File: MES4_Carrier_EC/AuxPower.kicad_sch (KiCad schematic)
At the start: 42 parts, among them J14 IMU 9V, J15 SERVO 24V, J16 SCREEN 5V, J17 SERVO UART, SW2 SS12D10G5, U10 URB2405YMD-20WR3, U9 URB2409S-10WR3

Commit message: One ground and a 4-layer board
- GND_24V merged into GND (ONE_GND in gen.py): every GND_24V power symbol
  becomes GND, net tie NT1 left out, notes reworded. Symbol UUIDs unchanged,
  so every footprint keeps its link.
- 4 layers, JLC04161H-7628 stackup (1.6 mm, ENIG): Top Signal / GND plane
  (In1) / +24V plane (In2) / Bottom Signal.
- Net classes: Out_3A (1.5 mm) for +24V_SRV, +5V_SCR, VBUS_SCR; +24V_AUX to
  24V_Power; +5V_SRV, +9V_IMU, IMU_9V to Power; INA236 shunt pattern fixed
  (Net-(U*-IN-)).
- J1's NPTH holes back to F&B.Cu as in its library footprint.

ERC 0, checks passed, DRC 11 silkscreen warnings, schematic parity clean.

Co-Authored-By: Claude Opus 5.5 <noreply@anthropic.com>
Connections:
- net GND_24V is gone; now on net GND: C26.2, C27.2, C28.2, C30.2, C31.2, C32.2, J15.2 (Pin_2), U10.2 (-Vin), U9.1 (GND)
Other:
- note added: "L2 10 µH (same part as L1) + C26 / C27: a pi filter of its own for the IMU and screen converters, so the screen's 20 W converter neither loads nor disturbs the logic supply (L1, Power sheet). Load at 24 V: IMU ≤ 0.5 A + screen ≤ 0.95 A ≈ 1.45 A; L2 is rated 2.1 A (2.9 A saturation). Both converters are isolated modules; on this board their input and output sides share the one GND (as the logic DC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"
- note removed: "L2 10 µH (same part as L1) + C26 / C27: a pi filter of its own for the IMU and screen converters, so the screen's 20 W converter neither loads nor disturbs the logic supply (L1, Power sheet). Load at 24 V: IMU ≤ 0.5 A + screen ≤ 0.95 A ≈ 1.45 A; L2 is rated 2.1 A (2.9 A saturation). Both converters are isolated: input side on GND_24V, output side on GND (same scheme as the logic DC/DC)."

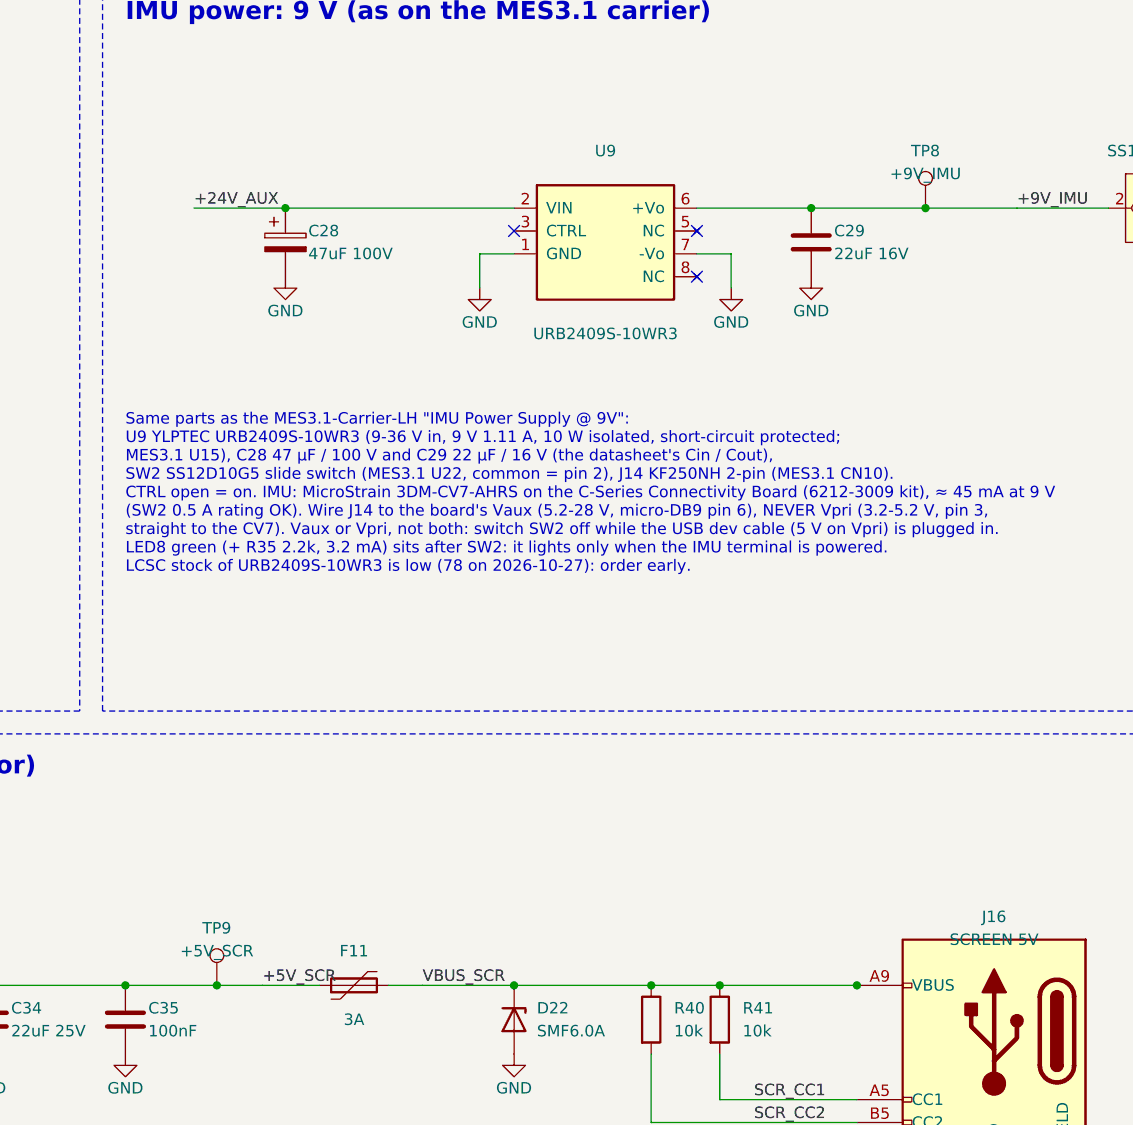
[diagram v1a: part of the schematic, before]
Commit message: Placement and silkscreen pass: ADS by the load-cell inputs, test points, logo
- Left column top to bottom: ADS1232 under J12/J13 (input filter toward the
  connectors), STDC14 + ESD grid, then the MES4-MCU slot moved down 22.3 mm;
  RESET (SW1) beside J1 with the 5 V socket caps C8/C9.
- Test points named by what they feed (TP_NAME in gen.py: 24V, 24V FILT,
  5V MAIN, 5V MCU, 3V3, 9V IMU, 5V SCREEN); bottom row in a Flasher-style
  rounded box, 24V/GND under the XT30, 5V SCREEN/GND by the screen USB-C.
- Supply LEDs centred between SW2 and the winch block; short knockout labels
  all one box size (drawn as cut-out silk shapes).
- + at the anode of every two-pin diode and LED; SW2 marked IMU PWR with
  OFF/ON (slider toward pin 1 = on); mounting-hole refs off the silkscreen.
- Sensor inputs in the column under L1/L2, U10 output caps against U10,
  servo support parts in the square by J17, FE-URT-2 J17/J15 label boxes,
  Monkey Robotics logo (43 x 9.3 mm) in the freed space.

ERC 0, DRC 14 silkscreen warnings (13 edge, J1 circle), schematic parity clean.

Co-Authored-By: Claude Opus 5.5 <noreply@anthropic.com>
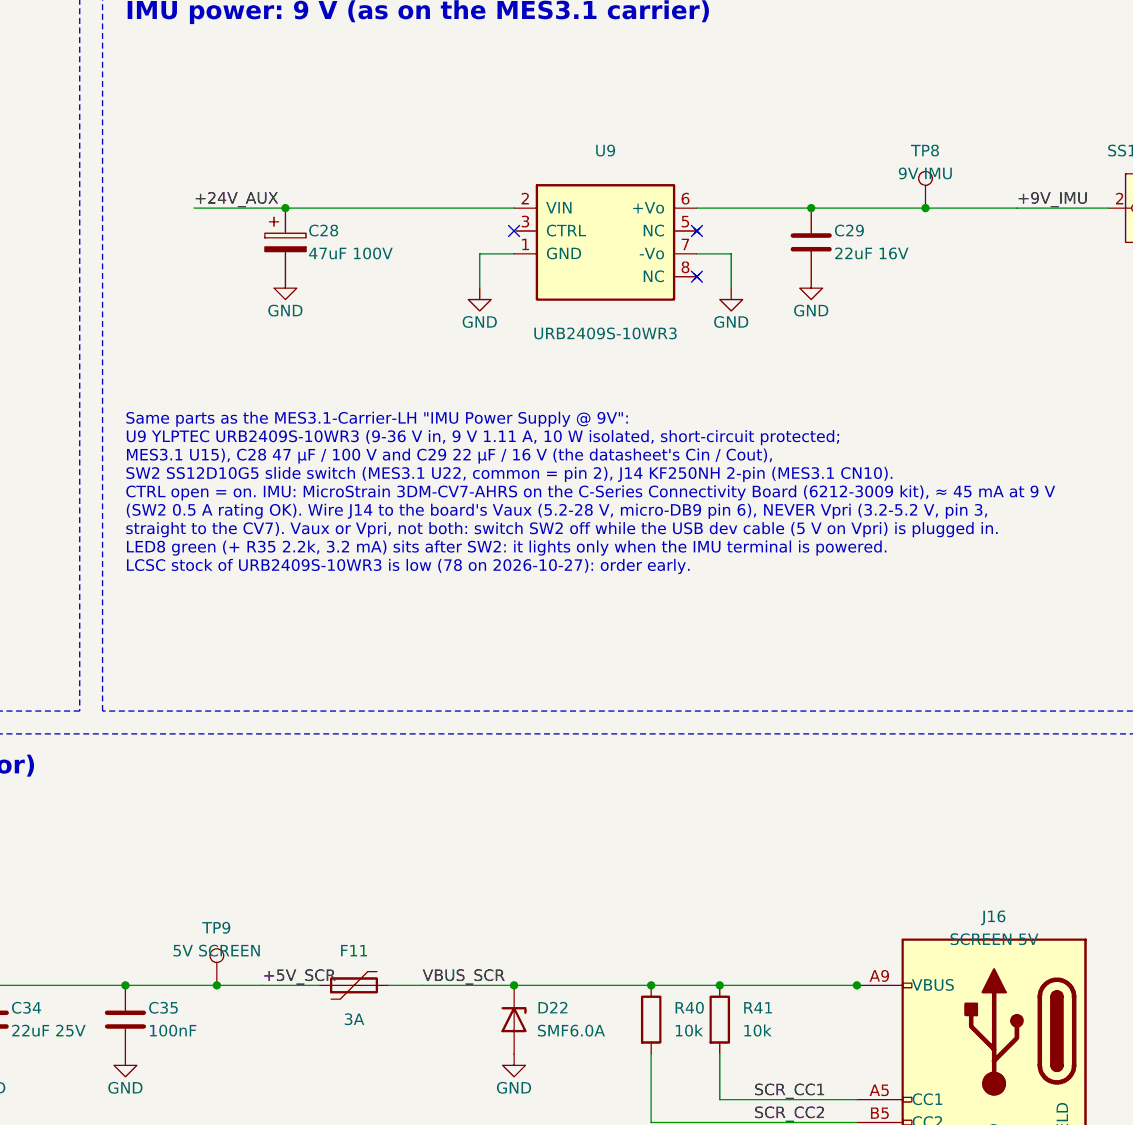
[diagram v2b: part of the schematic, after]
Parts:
- TP8: value +9V_IMU -> 9V IMU
- TP9: value +5V_SCR -> 5V SCREEN
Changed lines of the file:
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@@
 			(effects (font (size 1.27 1.27)))
 		)
-		(property "Value" "+9V_IMU"
+		(property "Value" "9V IMU"
 			(at 213.36 41.91 0)
 			(effects (font (size 1.27 1.27)))
@@
 			(effects (font (size 1.27 1.27)))
 		)
-		(property "Value" "+5V_SCR"
+		(property "Value" "5V SCREEN"
 			(at 134.62 128.27 0)
 			(effects (font (size 1.27 1.27)))

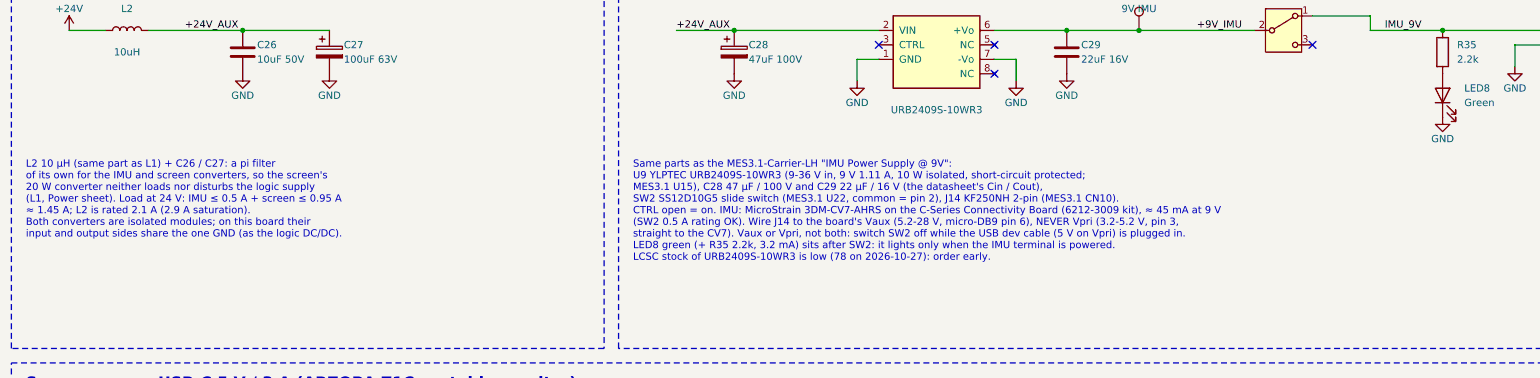
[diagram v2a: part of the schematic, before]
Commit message: Fix design review R3 findings: U9 part, stale LCSC fields, labels, J16
- B1: U9 is now YLPTEC URB2409S-6WR3 (C7468814, 9 V 6 W) on U1's
  footprint; the 10 W URB2409S-10WR3 isn't in JLC's assembly library.
  The production BOM had a 5 V module at U9 and the wrong SW2 because
  EasyEDA footprints carry an "LCSC Part" field the Fabrication Toolkit
  reads first: libs.py strips it (and the unprintable pin-1 dots it was
  copying back), and the new parts_sync.py syncs board footprints,
  values, fields and BOM flags from the schematic. TP1-TP9 and H2-H5
  are out of the BOM and CPL.
- M2 / L5: "5V LOAD CELL" across J12 / J13; "CANBUS" knockout by J4.
- B2: J16 moves 1.25 mm west so its mouth reaches the board edge.
- B8 / N6: README (one ground, U9, J16, labels, TPs), schematic notes
  and HANDOFF updated; 1:1 A4 print refreshed.
- DRC with parity at the 3 accepted J4 notes; nets, audit, DFM clean.
  production/ is stale until the Fabrication Toolkit is re-run.

Co-Authored-By: Claude Opus 5.5 <noreply@anthropic.com>
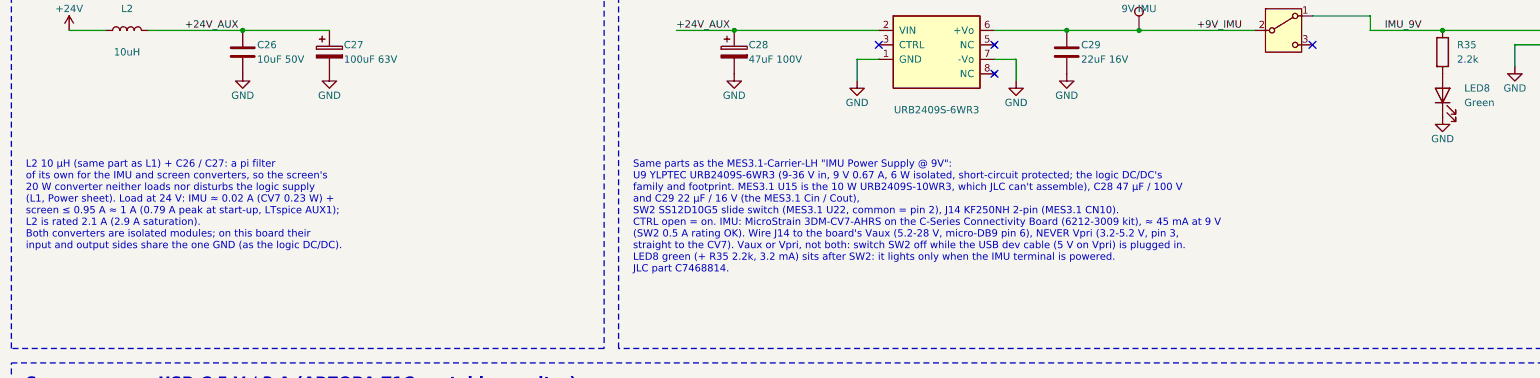
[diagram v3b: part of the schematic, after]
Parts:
- TP8, TP9: now left out of the parts list
- U9: value URB2409S-10WR3 -> URB2409S-6WR3; footprint MES4-Carrier-EC:PWRM-TH_YLPTEC_URBXXXXS-10WR3 -> MES4-Carrier-EC:PWRM-TH_YLPTEC_URXXXXXS-6WR3; symbol MES4-Carrier-EC:URB2409S-10WR3 -> MES4-Carrier-EC:URB2409S-6WR3; LCSC C7424703 -> C7468814
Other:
- note added: "L2 10 µH (same part as L1) + C26 / C27: a pi filter of its own for the IMU and screen converters, so the screen's 20 W converter neither loads nor disturbs the logic supply (L1, Power sheet). Load at 24 V: IMU ≈ 0.02 A (CV7 0.23 W) + screen ≤ 0.95 A ≈ 1 A (0.79 A peak at start-up, LTspice AUX1); L2 is rated 2.1 A (2.9 A saturation). Both converters are isolated modules; on this board their input 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"
- note added: "Same parts as the MES3.1-Carrier-LH "IMU Power Supply @ 9V": U9 YLPTEC URB2409S-6WR3 (9-36 V in, 9 V 0.67 A, 6 W isolated, short-circuit protected; the logic DC/DC's family and footprint. MES3.1 U15 is the 10 W URB2409S-10WR3, which JLC can't assemble), C28 47 µF / 100 V and C29 22 µF / 16 V (the MES3.1 Cin / Cout), SW2 SS12D10G5 slide switch (MES3.1 U22, common = pin 2), J14 KF250NH 2-pin (MES3.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"
- note removed: "L2 10 µH (same part as L1) + C26 / C27: a pi filter of its own for the IMU and screen converters, so the screen's 20 W converter neither loads nor disturbs the logic supply (L1, Power sheet). Load at 24 V: IMU ≤ 0.5 A + screen ≤ 0.95 A ≈ 1.45 A; L2 is rated 2.1 A (2.9 A saturation). Both converters are isolated modules; on this board their input and output sides share the one GND (as the logic DC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"
- note removed: "Same parts as the MES3.1-Carrier-LH "IMU Power Supply @ 9V": U9 YLPTEC URB2409S-10WR3 (9-36 V in, 9 V 1.11 A, 10 W isolated, short-circuit protected; MES3.1 U15), C28 47 µF / 100 V and C29 22 µF / 16 V (the datasheet's Cin / Cout), SW2 SS12D10G5 slide switch (MES3.1 U22, common = pin 2), J14 KF250NH 2-pin (MES3.1 CN10). CTRL open = on. IMU: MicroStrain 3DM-CV7-AHRS on the C-Series Connectivity Bo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"
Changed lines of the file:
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@@
 		(effects (font (size 1.27 1.27)) (justify left bottom))
 	)
-	(text "L2 10 µH (same part as L1) + C26 / C27: a pi filter\nof its own for the IMU and screen converters, so the screen's\n20 W converter neither loads nor disturbs the logic supply\n(L1, Power sheet). Load at 24 V: IMU ≤ 0.5 A + screen ≤ 0.95 A\n≈ 1.45 A; L2 is rated 2.1 A (2.9 A saturation).\nBoth converters are isolated modules; on this board their\ninput and output sides share the one GND (as the logic DC/DC)."
+	(text "L2 10 µH (same part as L1) + C26 / C27: a pi filter\nof its own for the IMU and screen converters, so the screen's\n20 W converter neither loads nor disturbs the logic supply\n(L1, Power sheet). Load at 24 V: IMU ≈ 0.02 A (CV7 0.23 W) +\nscreen ≤ 0.95 A ≈ 1 A (0.79 A peak at start-up, LTspice AUX1);\nL2 is rated 2.1 A (2.9 A saturation).\nBoth converters are isolated modules; on this board their\ninput and output sides share the one GND (as the logic DC/DC)."
 		(exclude_from_sim no)
 		(at 17.78 68.58 0)
@@
 		(stroke (width 0) (type default))
 	)
-	(text "Same parts as the MES3.1-Carrier-LH \"IMU Power Supply @ 9V\":\nU9 YLPTEC URB2409S-10WR3 (9-36 V in, 9 V 1.11 A, 10 W isolated, short-circuit protected;\nMES3.1 U15), C28 47 µF / 100 V and C29 22 µF / 16 V (the datasheet's Cin / Cout),\nSW2 SS12D10G5 slide switch (MES3.1 U22, common = pin 2), J14 KF250NH 2-pin (MES3.1 CN10).\nCTRL open = on. IMU: MicroStrain 3DM-CV7-AHRS on the C-Series Connectivity Board (6212-3009 kit), ≈ 45 mA at 9 V\n(SW2 0.5 A rating OK). Wire J14 to the board's Vaux (5.2-28 V, micro-DB9 pin 6), NEVER Vpri (3.2-5.2 V, pin 3,\nstraight to the CV7). Vaux or Vpri, not both: switch SW2 off while the USB dev cable (5 V on Vpri) is plugged in.\nLED8 green (+ R35 2.2k, 3.2 mA) sits after SW2: it lights only when the IMU terminal is powered.\nLCSC stock of URB2409S-10WR3 is low (78 on 2026-10-27): order early."
+	(text "Same parts as the MES3.1-Carrier-LH \"IMU Power Supply @ 9V\":\nU9 YLPTEC URB2409S-6WR3 (9-36 V in, 9 V 0.67 A, 6 W isolated, short-circuit protected; the logic DC/DC's\nfamily and footprint. MES3.1 U15 is the 10 W URB2409S-10WR3, which JLC can't assemble), C28 47 µF / 100 V\nand C29 22 µF / 16 V (the MES3.1 Cin / Cout),\nSW2 SS12D10G5 slide switch (MES3.1 U22, common = pin 2), J14 KF250NH 2-pin (MES3.1 CN10).\nCTRL open = on. IMU: MicroStrain 3DM-CV7-AHRS on the C-Series Connectivity Board (6212-3009 kit), ≈ 45 mA at 9 V\n(SW2 0.5 A rating OK). Wire J14 to the board's Vaux (5.2-28 V, micro-DB9 pin 6), NEVER Vpri (3.2-5.2 V, pin 3,\nstraight to the CV7). Vaux or Vpri, not both: switch SW2 off while the USB dev cable (5 V on Vpri) is plugged in.\nLED8 green (+ R35 2.2k, 3.2 mA) sits after SW2: it lights only when the IMU terminal is powered.\nJLC part C7468814."
 		(exclude_from_sim no)
 		(at 124.46 68.58 0)
@@
 	)
 	(symbol
-		(lib_id "MES4-Carrier-EC:URB2409S-10WR3")
+		(lib_id "MES4-Carrier-EC:URB2409S-6WR3")
 		(at 177.8 48.26 0)
 		(unit 1)
@@
 			(effects (font (size 1.27 1.27)))
 		)
-		(property "Value" "URB2409S-10WR3"
+		(property "Value" "URB2409S-6WR3"
 			(at 177.8 59.69 0)
 			(effects (font (size 1.27 1.27)))
 		)
-		(property "Footprint" "MES4-Carrier-EC:PWRM-TH_YLPTEC_URBXXXXS-10WR3"
+		(property "Footprint" "MES4-Carrier-EC:PWRM-TH_YLPTEC_URXXXXXS-6WR3"
 			(at 177.8 48.26 0)
 			(effects (font (size 1.27 1.27)) (hide yes))
 		)
-		(property "Datasheet" "https://www.lcsc.com/product-detail/C7424703.html"
+		(property "Datasheet" "https://www.lcsc.com/product-detail/C7468814.html"
 			(at 177.8 48.26 0)
 			(effects (font (size 1.27 1.27)) (hide yes))
 		)
-		(property "Description" "IMU supply, YLPTEC URB2409S-10WR3: 24 V to 9 V 1.11 A, 10 W isolated (as U15 on the MES3.1 carrier)"
+		(property "Description" "IMU supply, YLPTEC URB2409S-6WR3: 24 V to 9 V 0.67 A, 6 W isolated, SIP-8 (the logic DC/DC's family and footprint; the MES3.1 carrier's 10 W URB2409S-10WR3, C7424703, is not in JLC's assembly library)"
 			(at 177.8 48.26 0)
 			(effects (font (size 1.27 1.27)) (hide yes))
 		)
-		(property "LCSC" "C7424703"
+		(property "LCSC" "C7468814"
 			(at 177.8 48.26 0)
 			(effects (font (size 1.27 1.27)) (hide yes))
@@
 		(unit 1)
 		(exclude_from_sim no)
-		(in_bom yes)
+		(in_bom no)
 		(on_board yes)
 		(dnp no)
@@
 		(unit 1)
 		(exclude_from_sim no)
-		(in_bom yes)
-		(on_board yes)
-		(dnp no)
+		(in_bom no)
+		(on_board yes)
+		(dnp no)

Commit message: Fix design review R4 (CPL), add 3D models, STEP and the enclosure
Review R4:
- E1 (blocking): the Fabrication Toolkit turns every CP_Elec 180 deg, but
  JLC's footprints for C1/C5/C27/C28/C30/C32/C38 have + on the same side
  as ours, so all seven would have been fitted reversed. gen.py now sets
  FT Rotation Offset 180 on every CP_Elec part (the toolkit adds it to its
  own 180), so the CPL keeps the board rotation.
- E2: J5's FT Position Offset 0,9.7 put the XT30 10 mm off; JLC's origin
  is ours. Removed; parts_sync.py now drops FT fields the schematic no
  longer has.
- E3: parts_sync.py keeps H2-H5's empty LCSC field (KiCad 10 field parity).
- cpl_check.py rewritten as a gate: places JLC's own footprint where the
  CPL says, every JLC pad must land on our pads (pegs included), pin n on
  our pin n wherever the pattern also fits at another turn; only
  non-polar two-pad parts may sit 180 deg round. 177/181 pass, 0 to fix.
- production.sh: Fabrication Toolkit CLI, then the gate; deletes the
  order zip if it fails. production/ regenerated through it.

3D / STEP: EasyEDA STEP models placed onto their pads (J1 M.2, J16, K5/K6,
U1/U9, SW2), LCSC STEPs for the KF250 terminals and fuses, standoffs
converted from VRML (wrl2step.py); review/MES4_Carrier_EC.step.

Enclosure: two-part FDM box generated from the board (FreeCAD): M3
heat-set inserts, connector openings, LED light guides and labels, M5
side tabs, engraved logo, P1S tolerances, no supports. The 82 MB
assembly STEP is regenerated, not committed.

Co-Authored-By: Claude Opus 5.5 <noreply@anthropic.com>
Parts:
- C27, C28, C30, C32, C38: FT Rotation Offset (none) -> 180
- F11, F9: footprint Fuse:Fuse_2920_7451Metric -> MES4-Carrier-EC:Fuse_2920_7451Metric
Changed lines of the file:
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@@
+			(effects (font (size 1.27 1.27)) (hide yes))
+		)
+		(property "FT Rotation Offset" "180"
+			(at 71.12 49.53 0)
 			(effects (font (size 1.27 1.27)) (hide yes))
 		)
@@
 		)
 		(property "LCSC" "C48935391"
+			(at 142.24 49.53 0)
+			(effects (font (size 1.27 1.27)) (hide yes))
+		)
+		(property "FT Rotation Offset" "180"
 			(at 142.24 49.53 0)
 			(effects (font (size 1.27 1.27)) (hide yes))
@@
 			(effects (font (size 1.27 1.27)) (hide yes))
 		)
+		(property "FT Rotation Offset" "180"
+			(at 35.56 135.89 0)
+			(effects (font (size 1.27 1.27)) (hide yes))
+		)
 		(pin "1"
 		)
@@
 			(effects (font (size 1.27 1.27)))
 		)
-		(property "Footprint" "Fuse:Fuse_2920_7451Metric"
+		(property "Footprint" "MES4-Carrier-EC:Fuse_2920_7451Metric"
 			(at 149.86 132.08 0)
 			(effects (font (size 1.27 1.27)) (hide yes))
@@
 			(effects (font (size 1.27 1.27)) (hide yes))
 		)
+		(property "FT Rotation Offset" "180"
+			(at 256.54 181.61 0)
+			(effects (font (size 1.27 1.27)) (hide yes))
+		)
 		(pin "1"
 		)
@@
 			(effects (font (size 1.27 1.27)))
 		)
-		(property "Footprint" "Fuse:Fuse_2920_7451Metric"
+		(property "Footprint" "MES4-Carrier-EC:Fuse_2920_7451Metric"
 			(at 35.56 215.9 0)
 			(effects (font (size 1.27 1.27)) (hide yes))
@@
 			(at 71.12 219.71 0)
 			(effects (font (size 1.27 1.27)) (hide yes))
+		)
+		(property "FT Rotation Offset" "180"
+			(at 71.12 219.71 0)
+			(effects (font (size 1.27 1.27)) (hide yes))
